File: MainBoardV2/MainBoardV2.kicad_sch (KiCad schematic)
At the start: 21 parts, among them J10 Conn_01x04, J2 Conn_01x04, J4 Conn_01x04, J5 Conn_01x05, J6 Conn_01x02, J7 Conn_01x04, J8 Conn_01x04, J9 Conn_01x04, SW3 SW_DIP_x03, SW4 SW_DIP_x03, SW5 SW_DIP_x03, U1 ESP32-S3-WROOM-1, U2 ESP32-S3-DevKitC, U4 TEN20-2411WIN

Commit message: Finished V2
Finished V2, waiting for comfirmation for production
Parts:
- removed U1: ESP32-S3-WROOM-1, Espressif:ESP32-S3-WROOM-1, symbol ESP32:ESP32-S3-WROOM-1
- removed U4: TEN20-2411WIN, Converter_DCDC:Converter_DCDC_TRACO_TEN20-xxxx_THT, symbol Converter_DCDC:TEN20-2411WIN
- added C1, C2: C_Small, Capacitor_SMD:C_0805_2012Metric_Pad1.18x1.45mm_HandSolder, symbol Device:C_Small
- added D1, D3, D4: LED_Small, LED_SMD:LED_1206_3216Metric_Pad1.42x1.75mm_HandSolder, symbol Device:LED_Small
- added H1, H2, H3, H4: MountingHole, MountingHole:MountingHole_3.2mm_M3_DIN965_Pad, symbol Mechanical:MountingHole
- added J1: Conn_01x02, TerminalBlock:TerminalBlock_Altech_AK300-2_P5.00mm, symbol Connector_Generic:Conn_01x02
- added J11, J16, J17: Conn_01x02, Connector_PinHeader_2.54mm:PinHeader_1x02_P2.54mm_Vertical, symbol Connector_Generic:Conn_01x02
- added J12, J13, J14, J15, J18, J19, J20, J21, J22, J3: Conn_01x03, Connector_PinHeader_2.54mm:PinHeader_1x03_P2.54mm_Vertical, symbol Connector_Generic:Conn_01x03
- added J23: Conn_01x05, Connector_JST:JST_XH_B5B-XH-A_1x05_P2.50mm_Vertical, symbol Connector_Generic:Conn_01x05
- added R1: R, Resistor_THT:R_Axial_DIN0204_L3.6mm_D1.6mm_P5.08mm_Vertical, symbol Device:R
- added R2: R, Resistor_THT:R_Axial_DIN0204_L3.6mm_D1.6mm_P7.62mm_Horizontal, symbol Device:R
- added R3, R4, R5: R_Small, Resistor_SMD:R_1206_3216Metric_Pad1.30x1.75mm_HandSolder, symbol Device:R_Small
- added U1: AMS1117-3.3, Package_TO_SOT_SMD:SOT-223-3_TabPin2, symbol Regulator_Linear:AMS1117-3.3
- J10, J2, J4: footprint Connector_JST:JST_XH_B4B-XH-A_1x04_P2.50mm_Vertical -> Connector_Molex:Molex_KK-254_AE-6410-04A_1x04_P2.54mm_Vertical
- SW3, SW4, SW5: footprint Button_Switch_SMD:SW_DIP_SPSTx03_Slide_9.78x9.8mm_W8.61mm_P2.54mm -> Button_Switch_THT:SW_DIP_SPSTx03_Slide_9.78x9.8mm_W7.62mm_P2.54mm
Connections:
- net -BATT is gone; now on net +12V: J6.1 (Pin_1)
- net +12V: now also J16.1 (Pin_1), J16.2 (Pin_2), R4.2; no longer J6.2 (Pin_2)
- net EN: now also U2.14 (GPIO46)
- net GND: now also J6.2 (Pin_2), J7.4 (Pin_4), J8.4 (Pin_4), J9.4 (Pin_4), C1.2, C2.2, D1.1 (K), D3.1 (K), D4.1 (K), J1.1 (Pin_1), J12.1 (Pin_1), J13.1 (Pin_1), J14.1 (Pin_1), J17.1 (Pin_1), J17.2 (Pin_2), J19.1 (Pin_1), J20.1 (Pin_1), J21.1 (Pin_1), J22.1 (Pin_1), J23.1 (Pin_1), J3.1 (Pin_1), U1.1 (GND); no longer J7.1 (Pin_1), J8.1 (Pin_1), J9.1 (Pin_1)
- net SCL: now also R1.2
- net SDA: now also R2.2
- net +3.3V: now reaches U2.1 (3V3), U2.2 (3V3)
- net +3.3V: now also R1.1, R2.1
- net at U2.28 (GPIO47): now also J20.3 (Pin_3)
- net at U2.29 (GPIO48): now also J21.3 (Pin_3)
- net at U2.30 (GPIO45): now also J19.3 (Pin_3)
- net GP35: now reaches U2.32 (GPIO35)
- net GP35: now also J14.3 (Pin_3)
- net GP36: now reaches U2.33 (GPIO36)
- net GP36: now also J13.3 (Pin_3)
- net GP37: now reaches U2.34 (GPIO37)
- net GP37: now also J12.3 (Pin_3)
- net GP38: now reaches U2.35 (GPIO38)
- net GP38: now also J3.3 (Pin_3)
- net at U2.36 (GPIO39/MTCK): now also J23.5 (Pin_5)
- net at U2.37 (GPIO40/MTDO): now also J23.4 (Pin_4)
- net at U2.38 (GPIO41/MTDI): now also J23.3 (Pin_3)
- net at U2.39 (GPIO42/MTMS): now also J23.2 (Pin_2)
- net GP2: now reaches U2.40 (GPIO2/ADC1_CH1)
- net GP2: now also J11.2 (Pin_2)
- net GP1: now reaches U2.41 (GPIO1/ADC1_CH0)
- net GP1: now also J11.1 (Pin_1)
- net at U2.42 (GPIO44/U0RXD): now also J22.3 (Pin_3)
- net at U2.43 (GPIO43/U0TXD): now also J22.2 (Pin_2)
- net 5VPower renamed +5V
- net +5V: now also C1.1, J1.2 (Pin_2), J15.3 (Pin_3), J18.3 (Pin_3), R3.1, U1.3 (VI); no longer J7.4 (Pin_4), J8.4 (Pin_4), J9.4 (Pin_4)
- new net: J18.2 (Pin_2), J7.1 (Pin_1), J8.1 (Pin_1), J9.1 (Pin_1)
- new net: J12.2 (Pin_2), J13.2 (Pin_2), J14.2 (Pin_2), J15.2 (Pin_2), J19.2 (Pin_2), J20.2 (Pin_2), J21.2 (Pin_2), J3.2 (Pin_2)
- new net: D1.2 (A), R3.2
- new net: D3.2 (A), R4.1
- new net: D4.2 (A), R5.2
- new net +3.3VP: C2.1, J15.1 (Pin_1), J18.1 (Pin_1), R5.1, U1.2 (VO)
- no-connect marks 6 -> 9
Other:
- note removed: "relier Fault au micro ou led."
- moved on the sheet: A1, A2, A3, C7, C8, C9, D2, J10, J2, J4, J5, J6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

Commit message: Finishing touches, Added Ticker Lines
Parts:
- added Tir.1: Conn_01x02, Connector_JST:JST_XH_B2B-XH-A_1x02_P2.50mm_Vertical, symbol Connector_Generic:Conn_01x02
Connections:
- net GND: now also Tir.1.1 (Pin_1)
- net at U2.12 (GPIO8/ADC1_CH7): now also Tir.1.2 (Pin_2)
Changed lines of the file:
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@@
+    (stroke (width 0) (type default))
+  )
+  (wire (pts (xy 141.605 66.04) (xy 163.83 66.04))
     (stroke (width 0) (type default))
   )
@@
     )
   )
+  (symbol (lib_id "power:GND") (at 163.83 63.5 270) (unit 1)
+    (in_bom yes) (on_board yes) (dnp no) (fields_autoplaced)
+    (property "Reference" "#PWR021" (at 157.48 63.5 0)
+      (effects (font (size 1.27 1.27)) hide)
+    )
+    (property "Value" "GND" (at 160.02 63.5 90)
+      (effects (font (size 1.27 1.27)) (justify right))
+    )
+    (property "Footprint" "" (at 163.83 63.5 0)
+      (effects (font (size 1.27 1.27)) hide)
+    )
+    (property "Datasheet" "" (at 163.83 63.5 0)
+      (effects (font (size 1.27 1.27)) hide)
+    )
+    (pin "1")
+    (instances
+      (project "MainBoardV2"
+        (path "/ccdda621-e361-4147-9a57-71374655ba08"
+          (reference "#PWR021") (unit 1)
+        )
+      )
+    )
+  )
   (symbol (lib_id "Connector_Generic:Conn_01x05") (at 190.5 93.98 180) (unit 1)
     (in_bom yes) (on_board yes) (dnp no) (fields_autoplaced)
@@
         )
       )
+    )
+  )
+  (symbol (lib_id "Connector_Generic:Conn_01x02") (at 168.91 63.5 0) (unit 1)
+    (in_bom yes) (on_board yes) (dnp no) (fields_autoplaced)
+    (property "Reference" "Tir.1" (at 171.45 63.5 0)
+      (effects (font (size 1.27 1.27)) (justify left))
+    )
+    (property "Value" "Conn_01x02" (at 171.45 66.04 0)
+      (effects (font (size 1.27 1.27)) (justify left))
+    )
+    (property "Footprint" "Connector_JST:JST_XH_B2B-XH-A_1x02_P2.50mm_Vertical" (at 168.91 63.5 0)
+      (effects (font (size 1.27 1.27)) hide)
+    )
+    (property "Datasheet" "~" (at 168.91 63.5 0)
+      (effects (font (size 1.27 1.27)) hide)
+    )
+    (pin "1")
+    (pin "2")
+    (instances
+      (project "MainBoardV2"
+        (path "/ccdda621-e361-4147-9a57-71374655ba08"
+          (reference "Tir.1") (unit 1)
+        )
+      )

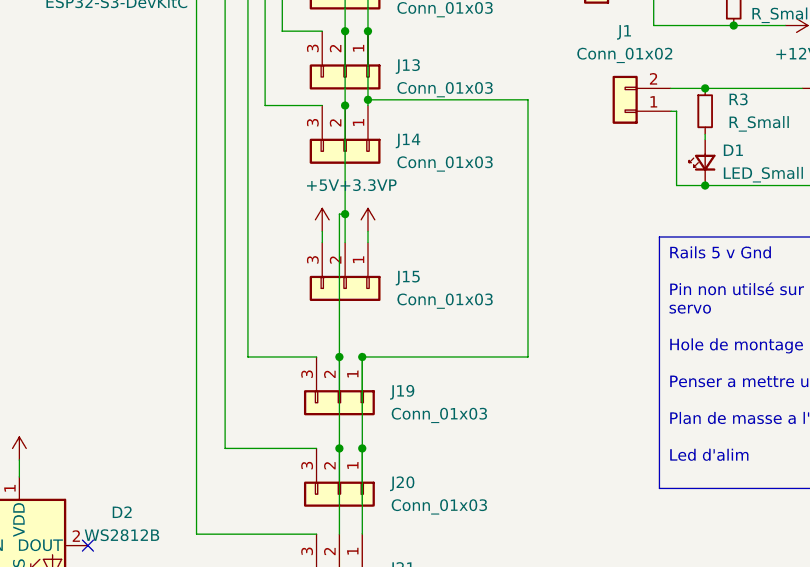
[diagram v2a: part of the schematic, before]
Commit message: Last desing of V2, and creation of V3
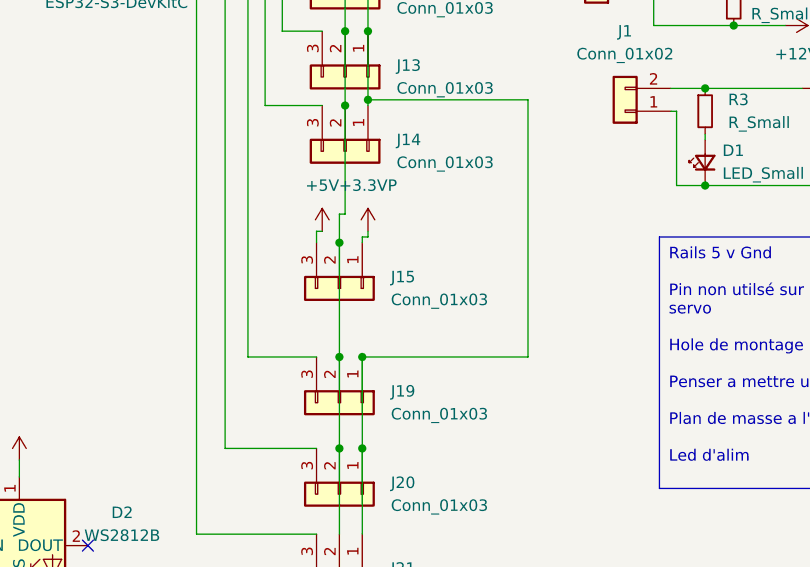
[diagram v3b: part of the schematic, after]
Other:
- moved on the sheet: J15
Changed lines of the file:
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@@
   (junction (at 20.955 56.515) (diameter 0) (color 0 0 0 0)
   )
-  (junction (at 159.385 137.16) (diameter 0) (color 0 0 0 0)
+  (junction (at 158.75 140.335) (diameter 0) (color 0 0 0 0)
   )
   (junction (at 20.955 179.07) (diameter 0) (color 0 0 0 0)
@@
     (stroke (width 0) (type default))
   )
-  (wire (pts (xy 161.925 139.065) (xy 161.925 140.335))
+  (wire (pts (xy 161.29 139.7) (xy 161.29 140.335))
     (stroke (width 0) (type default))
   )
@@
     (stroke (width 0) (type default))
   )
+  (wire (pts (xy 156.21 139.065) (xy 156.845 139.065))
+    (stroke (width 0) (type default))
+  )
   (wire (pts (xy 200.025 50.165) (xy 195.58 50.165))
     (stroke (width 0) (type default))
@@
     (stroke (width 0) (type default))
   )
-  (wire (pts (xy 156.845 139.065) (xy 156.845 140.335))
+  (wire (pts (xy 156.21 139.065) (xy 156.21 140.335))
     (stroke (width 0) (type default))
   )
@@
     (stroke (width 0) (type default))
   )
+  (wire (pts (xy 158.75 137.16) (xy 159.385 137.16))
+    (stroke (width 0) (type default))
+  )
   (wire (pts (xy 40.64 61.595) (xy 43.815 61.595))
     (stroke (width 0) (type default))
@@
     (stroke (width 0) (type default))
   )
+  (wire (pts (xy 161.29 139.7) (xy 161.925 139.7))
+    (stroke (width 0) (type default))
+  )
   (wire (pts (xy 67.945 45.085) (xy 64.135 45.085))
     (stroke (width 0) (type default))
@@
     (stroke (width 0) (type default))
   )
-  (wire (pts (xy 158.75 137.16) (xy 159.385 137.16))
-    (stroke (width 0) (type default))
-  )
   (wire (pts (xy 199.39 133.985) (xy 196.215 133.985))
     (stroke (width 0) (type default))
@@
     (stroke (width 0) (type default))
   )
+  (wire (pts (xy 161.925 139.7) (xy 161.925 139.065))
+    (stroke (width 0) (type default))
+  )
   (wire (pts (xy 22.225 102.235) (xy 45.085 102.235))
     (stroke (width 0) (type default))
@@
     (stroke (width 0) (type default))
   )
-  (wire (pts (xy 159.385 137.16) (xy 159.385 140.335))
+  (wire (pts (xy 158.75 137.16) (xy 158.75 140.335))
     (stroke (width 0) (type default))
   )
@@
     (stroke (width 0) (type default))
   )
-  (wire (pts (xy 158.75 153.035) (xy 158.75 137.16))
+  (wire (pts (xy 158.75 153.035) (xy 158.75 140.335))
     (stroke (width 0) (type default))
   )
@@
     )
   )
-  (symbol (lib_id "Connector_Generic:Conn_01x03") (at 159.385 145.415 270) (unit 1)
+  (symbol (lib_id "Connector_Generic:Conn_01x03") (at 158.75 145.415 270) (unit 1)
     (in_bom yes) (on_board yes) (dnp no) (fields_autoplaced)
-    (property "Reference" "J15" (at 165.1 144.145 90)
+    (property "Reference" "J15" (at 164.465 144.145 90)
       (effects (font (size 1.27 1.27)) (justify left))
     )
-    (property "Value" "Conn_01x03" (at 165.1 146.685 90)
+    (property "Value" "Conn_01x03" (at 164.465 146.685 90)
       (effects (font (size 1.27 1.27)) (justify left))
     )
-    (property "Footprint" "Connector_PinHeader_2.54mm:PinHeader_1x03_P2.54mm_Vertical" (at 159.385 145.415 0)
+    (property "Footprint" "Connector_PinHeader_2.54mm:PinHeader_1x03_P2.54mm_Vertical" (at 158.75 145.415 0)
       (effects (font (size 1.27 1.27)) hide)
     )
-    (property "Datasheet" "~" (at 159.385 145.415 0)
+    (property "Datasheet" "~" (at 158.75 145.415 0)
       (effects (font (size 1.27 1.27)) hide)
     )
